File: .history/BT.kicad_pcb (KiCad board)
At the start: 4 copper layers, 55 x 40 mm, 91 parts, among them J1 Conn_01x05_Pin, J2 Conn_01x03_Pin, J3 S6B-PH-K-S, J4 Boxed_Header_02x03_SMT, K1 AGQ200S12Z, Q1 BSS123, U1 PCM5100A, U2 ESP32-WROOM-32U, U3 TLV4888DR, U4 TLVM23615RDNR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

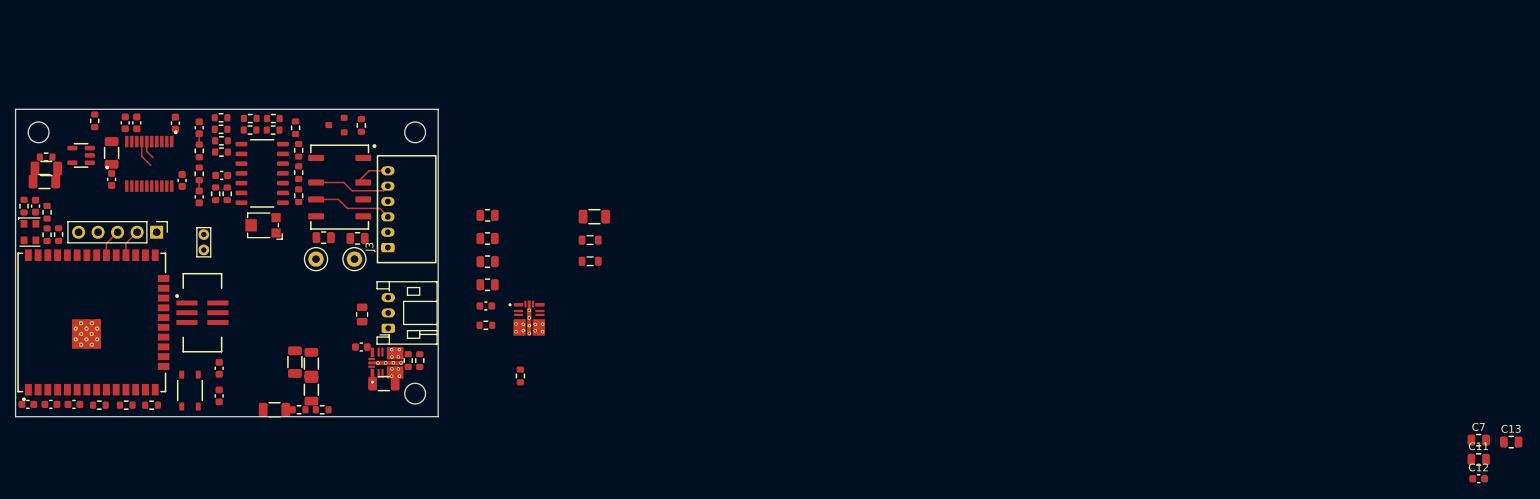
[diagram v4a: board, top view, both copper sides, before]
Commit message: rough placement PSU
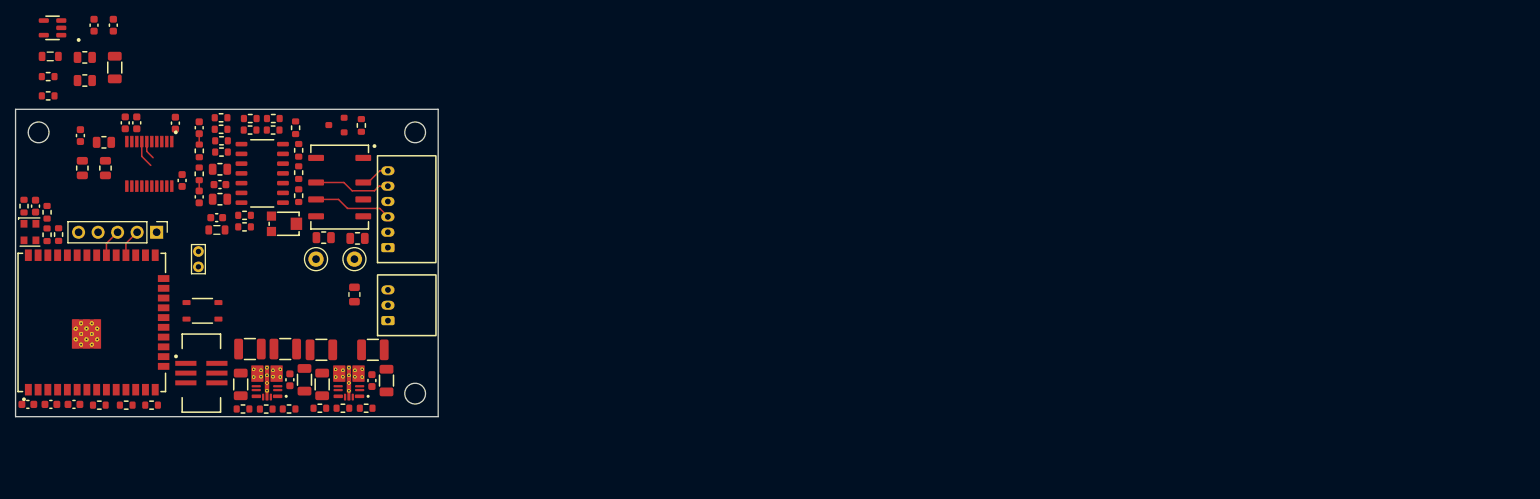
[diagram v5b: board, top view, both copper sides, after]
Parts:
- removed RV1: 10K, Potentiometer_SMD:Potentiometer_Bourns_TC33X_Vertical
- added R33: 10K, NRD_R_Var:TC33X-2, F.Cu at (155.8, 90.6)
- C24, C25, C29, C30: footprint NRD_CAP:C_1206 -> NRD_CAP:C_1210
- J2: value Conn_01x03_Pin -> S3B-PH-K-S; footprint Connector_JST:JST_PH_S3B-PH-K_1x03_P2.00mm_Horizontal -> NRD_CON:S3B-PH-K-S
- S1: value ~ -> 434123025826
- moved C12 187.4 mm to (129.1, 79.1), turned to 90 degrees
- moved C13 186.4 mm to (132.4, 83.4), turned to 90 degrees
- moved C11 185.6 mm to (129.4, 83.4), turned to 90 degrees
- moved C7 183.1 mm to (132.2, 80.0)
- moved FB2 74.2 mm to (125.2, 68.8)
- moved R32 64.3 mm to (124.9, 74.0)
- moved C22 56.3 mm to (129.7, 69.0)
- moved C33 56.3 mm to (129.7, 72.0)
- moved R31 56.1 mm to (124.9, 71.5)
- moved C31 50.9 mm to (130.9, 64.8)
- moved FB4 48.7 mm to (146.9, 91.4), turned to 180 degrees
- moved C32 46.7 mm to (133.4, 64.8)
- moved R19 45.2 mm to (156.3, 114.7), turned to 0 degrees
- moved C20 42.8 mm to (167.1, 111.0), turned to 90 degrees
- moved C19 42.6 mm to (158.3, 110.9), turned to 90 degrees
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
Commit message: replaced all components by library parts
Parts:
- removed C34: 2.2uF, NRD_CAP:C_0805
- removed FB2, FB4: 4k7@100MHz, Inductor_SMD:L_0805_2012Metric
- added D1: VSSAF5N50-M3/6B, NRD_Diodes:VSSAF5N50, F.Cu at (165.7, 71.8)
- added L1: 10uH, NRD_IND:74479777310, F.Cu at (184.9, 90.9)
- added L2: 10uH, NRD_IND:74479777310, F.Cu at (184.9, 94.0)
- added L3: 10uH, NRD_IND:74479777310, F.Cu at (184.9, 97.1)
- added L4: 10uH, NRD_IND:74479777310, F.Cu at (184.9, 100.2)
- added R34: 10K, NRD_RES:R_0603, F.Cu at (180.9, 98.1)
- added R35: 1K, NRD_RES:R_0603, F.Cu at (180.9, 100.6)
- added TP4: 5001, NRD_MISC:500x, F.Cu at (189.1, 91.4)
- added TP5: 5001, NRD_MISC:500x, F.Cu at (189.1, 95.5)
- C22: value 2.2uF -> 100nF; footprint NRD_CAP:C_0805 -> NRD_CAP:C_0603
- F1: value Fuse -> SF-1206S050-2; footprint Fuse:Fuse_0805_2012Metric -> NRD_Fuse:SF-1206S
- J1: value Conn_01x05_Pin -> 61300511121; footprint Connector_PinHeader_2.54mm:PinHeader_1x05_P2.54mm_Vertical -> NRD_PinHeader:61300511121
- K1: value AGQ200S12Z -> AGQ200A12Z; footprint NRD_Relays:AGQ200Sxxx -> NRD_Relays:AGQ200Axxx
- M1: renamed from H1; value MountingHole -> Mounting_Hole_2.7mm_Unplated; footprint MountingHole:MountingHole_2.7mm_M2.5_ISO7380 -> NRD_MECH:Mounting_Hole_2.7mm_Unplated
- M2: renamed from H2; value MountingHole -> Mounting_Hole_2.7mm_Unplated; footprint MountingHole:MountingHole_2.7mm_M2.5_ISO7380 -> NRD_MECH:Mounting_Hole_2.7mm_Unplated
- M3: renamed from H3; value MountingHole -> Mounting_Hole_2.7mm_Unplated; footprint MountingHole:MountingHole_2.7mm_M2.5_ISO7380 -> NRD_MECH:Mounting_Hole_2.7mm_Unplated
- TP1: value TestPoint -> 5001; footprint TestPoint:TestPoint_Bridge_Pitch2.0mm_Drill0.7mm -> NRD_MISC:500x
- TP2, TP3: value TestPoint -> 5001; footprint TestPoint:TestPoint_Loop_D2.50mm_Drill1.0mm -> NRD_MISC:500x
- moved C33 66.4 mm to (193.4, 90.8)
- moved R31 60.0 mm to (180.9, 93.1)
- moved R32 60.0 mm to (180.9, 95.6)
- moved C22 55.5 mm to (180.9, 90.6)
- moved J1 3.70 mm to (135.9, 89.8), turned to 0 degrees
- moved C25 2.10 mm to (162.6, 107.0)
- moved J2 0.10 mm to (171.7, 101.1)
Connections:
- net /DAC_MUTE renamed /DAC_MUTEn
- net Net-(U6-ADJ) renamed /+3V3A_FB
- C21 pad 1: Net-(U6-VOUT) -> /+3V3A_OUT
- C22 pad 1: Net-(U6-VOUT) -> /Button
- J2 pad 2: /Button -> Net-(J2-Pin_2)
- R31 pad 1: Net-(U6-VOUT) -> /+3V3A_OUT
- R7 pad 2: GND -> +3V3
- U6 pad 5: Net-(U6-VOUT) -> /+3V3A_OUT
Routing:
- net /DIN: track 3.59 -> 0.00 mm
- net /BCK: track 0.00 -> 3.59 mm

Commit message: started layout
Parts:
- removed TP4, TP5: 5001, NRD_MISC:500x
- moved C33 62.1 mm to (132.7, 77.7), turned to 90 degrees
- moved L3 59.0 mm to (128.6, 79.5), turned to 90 degrees
- moved L4 58.1 mm to (130.7, 79.5), turned to -90 degrees
- moved R31 52.6 mm to (129.1, 84.1)
- moved R34 50.5 mm to (139.5, 69.3)
- moved R32 50.2 mm to (132.0, 84.1)
- moved C22 49.1 mm to (137.3, 113.2)
- moved R35 48.3 mm to (134.3, 113.2)
- moved L2 38.1 mm to (147.3, 87.9)
- moved L1 37.7 mm to (147.3, 91.4), turned to 180 degrees
- moved R6 32.8 mm to (166.0, 103.1), turned to 180 degrees
- moved R17 20.9 mm to (169.4, 106.2), turned to 180 degrees
- moved C31 20.2 mm to (122.8, 83.2)
- moved C17 19.1 mm to (149.9, 109.3), turned to -90 degrees
- moved C11 19.0 mm to (144.0, 71.1)
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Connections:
- net Net-(J2-Pin_1) renamed /LED_CON
- net Net-(J2-Pin_2) renamed /BUTTON_CON
- net Net-(U4-FB) renamed /FB_+3V3
- J1 pad 2: /LRCK -> /BCK
- J1 pad 4: /BCK -> /LRCK
- U2 pad 28: /BCK -> /LRCK
- U2 pad 29: unconnected-(U2-IO5-Pad29) -> /DIN
- U2 pad 30: /LRCK -> unconnected-(U2-IO18-Pad30)
- U2 pad 31: /DIN -> /BCK
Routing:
- net Net-(C14-Pad2): track 0.00 -> 42.2 mm, vias 0 -> 2
- net +6V: track 0.00 -> 40.1 mm, vias 0 -> 3
- net GND: track 0.00 -> 38.0 mm, vias 0 -> 32
- net /ESP_EN: track 0.00 -> 36.2 mm, vias 0 -> 3
- net +12V: track 0.00 -> 34.5 mm, vias 0 -> 2
- net /ESP_RXD0: track 0.00 -> 30.2 mm
- net /ESP_TXD0: track 0.00 -> 26.7 mm
- net +3V3: track 0.00 -> 26.5 mm, vias 0 -> 8
- net /ESP_IO0: track 0.00 -> 21.5 mm
- net Net-(C8-Pad1): track 1.40 -> 21.0 mm, vias 0 -> 2
- net Net-(R25-Pad1): track 0.00 -> 18.6 mm, vias 0 -> 2
- net Net-(U3B-+): track 0.00 -> 15.9 mm, vias 0 -> 2
- net /KL30: track 0.00 -> 12.0 mm
- net /SCK: track 0.00 -> 11.8 mm, vias 0 -> 1
- net Net-(U3C-+): track 0.00 -> 10.1 mm
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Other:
- board text added: "+3V3"
- board text added: "BCK"
- board text added: "DIN"
- board text added: "GND"
- board text added: "LRCK"

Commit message: almost finished layout. Something is still off in the design rules
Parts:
- J2: value S3B-PH-K-S -> Conn_01x03_Pin
- M1, M2, M3: value Mounting_Hole_2.7mm_Unplated -> (none)
- S1: value 434123025826 -> Untitled
- moved R34 22.8 mm to (128.0, 88.9), turned to -90 degrees
- moved C12 21.9 mm to (138.8, 88.2), turned to 180 degrees
- moved C13 17.8 mm to (142.0, 88.2), turned to 0 degrees
- moved C7 12.5 mm to (140.1, 78.3), turned to 180 degrees
- moved C11 9.24 mm to (137.4, 77.6)
- moved TP1 8.36 mm to (152.8, 95.2)
- moved J1 2.47 mm to (135.9, 91.0)
- moved R15 1.20 mm to (125.0, 87.0)
- moved C8 0.85 mm to (144.9, 89.0)
- moved R6 0.83 mm to (166.2, 102.3), turned to 90 degrees
- moved C5 0.73 mm to (122.3, 113.9)
- moved C6 0.73 mm to (125.3, 113.9)
- moved C10 0.73 mm to (128.3, 113.9), turned to 180 degrees
- moved R3 0.73 mm to (131.3, 113.9)
- moved R35 0.73 mm to (134.3, 113.9)
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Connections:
- C3 pad 1: +3.3VA -> +3V3A
- C4 pad 1: +3.3VA -> +3V3A
- U1 pad 8: +3.3VA -> +3V3A
- U2 pad 10: /DAC_FMT -> unconnected-(U2-IO25-Pad10)
- U2 pad 30: unconnected-(U2-IO18-Pad30) -> /DAC_FLT
- U2 pad 33: /DAC_FLT -> /DAC_FMT
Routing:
- net /SW_TO_BT_AUDIO: track 0.00 -> 77.0 mm, vias 0 -> 2
- net /BUTTON_CON: track 1.01 -> 42.4 mm
- net /LED: track 0.00 -> 37.6 mm, vias 0 -> 2
- net GND: track 38.0 -> 73.0 mm, vias 32 -> 58
- net /DAC_MCLK_EN: track 0.00 -> 28.4 mm, vias 0 -> 2
- net /DAC_MUTEn: track 0.00 -> 26.3 mm, vias 0 -> 3
- net /DAC_DMP: track 0.00 -> 18.7 mm
- net /DAC_FMT: track 0.00 -> 16.5 mm
- net Net-(R24-Pad1): track 2.00 -> 17.6 mm, vias 0 -> 2
- net /DAC_FLT: track 0.00 -> 13.5 mm, vias 0 -> 2
- net /MCLK: track 0.00 -> 12.1 mm, vias 0 -> 2
- net +3V3: track 26.5 -> 33.7 mm, vias 8 -> 12
- net /SCK: track 11.8 -> 17.6 mm, vias 1 -> 2
- net /+3V3A_FB: track 0.00 -> 5.28 mm
- net Net-(U1-LDOO): track 0.00 -> 3.78 mm
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- added copper zone on F.Cu, net +12V
- added copper zone on F.Cu, net +3V3
- added copper zone on In2.Cu, net +3V3
- added copper zone on F.Cu, net +3V3A
- added copper zone on F.Cu, net /+3V3A_OUT
- added copper zone on B.Cu, net GND
- added copper zone on F.Cu, net GND
- added copper zone on In1.Cu, net GND
- added copper zone on F.Cu, net Net-(C32-Pad1)
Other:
- board text removed: "+3V3"
- board text removed: "BCK"
- board text removed: "DIN"
- board text removed: "GND"
- board text removed: "LRCK"
